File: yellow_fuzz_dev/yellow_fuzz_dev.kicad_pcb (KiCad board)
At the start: 2 copper layers, 148 parts, among them CON1 SN49B12B, J1 PJ-202A, J2 RA49B11, Q1 DMN2041L, Q10 BC817-25-TP, Q11 NSVJ3910SB3T1GOSCT-ND, Q12 BC817-25-TP, Q13 BC817-25-TP, Q14 NSVJ3910SB3T1GOSCT-ND, Q2 NSVJ3910SB3T1GOSCT-ND, Q3 DMN2041L, Q4 NSVJ3910SB3T1GOSCT-ND, Q5 BC817-25-TP, Q6 BC817-25-TP, Q7 BC817-25-TP, Q8 BC817-25-TP, Q9 BC817-25-TP, SW1 SW_SP3T_A24JP, SW2 SW_SP3T_A24JP, SW3 SW_SP3T_A24JP, SW4 SW_SPST_A11JP, SW5 SW_SPST_A11JP, U1 TL072CP, U2 TL072CP, U3 TL072CP, U4 TL072CP

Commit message: added 3d to connector and DIP footprints, moved to project lib, updated PCB
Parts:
- removed CON1: SN49B12B, digikey:Headphone_Jack_6.35mm_SN49B12B
- removed POT2, POT3: 3362P-1-102TLF, yellow_fuzz_dev:3362P-1-102TLF
- added C1: 1u, Capacitor_THT:CP_Radial_D4.0mm_P1.50mm, F.Cu at (350.5, 99.1)
- added C11: 100u, Capacitor_THT:CP_Radial_D5.0mm_P2.00mm, F.Cu at (330.9, 106.1)
- added C12: 100u, Capacitor_THT:CP_Radial_D5.0mm_P2.00mm, F.Cu at (337.5, 99.6)
- added C15: 10u, Capacitor_THT:CP_Radial_D5.0mm_P2.00mm, F.Cu at (330.9, 112.7)
- added C17: 10u, Capacitor_THT:CP_Radial_D5.0mm_P2.00mm, F.Cu at (337.5, 106.1)
- added C19: 1u, Capacitor_THT:CP_Radial_D4.0mm_P1.50mm, F.Cu at (356.1, 99.1)
- added C22: 220n, Capacitor_THT:CP_Radial_D5.0mm_P2.00mm, F.Cu at (344.2, 99.6)
- added C26: 1u, Capacitor_THT:CP_Radial_D4.0mm_P1.50mm, F.Cu at (350.5, 104.6)
- added C34: 10u, Capacitor_THT:CP_Radial_D5.0mm_P2.00mm, F.Cu at (337.5, 112.7)
- added C36: 1u, Capacitor_THT:CP_Radial_D4.0mm_P1.50mm, F.Cu at (343.9, 112.2)
- added C37: 10u, Capacitor_THT:CP_Radial_D5.0mm_P2.00mm, F.Cu at (344.2, 106.1)
- added C38: 220n, Capacitor_THT:CP_Radial_D5.0mm_P2.00mm, F.Cu at (354.9, 105.6)
- added C43: 1u, Capacitor_THT:CP_Radial_D4.0mm_P1.50mm, F.Cu at (354.6, 111.7)
- added C46: 1u, Capacitor_THT:CP_Radial_D4.0mm_P1.50mm, F.Cu at (360.2, 111.7)
- added C50: 10u, Capacitor_THT:CP_Radial_D5.0mm_P2.00mm, F.Cu at (361.6, 105.6)
- added C8: 100u, Capacitor_THT:CP_Radial_D5.0mm_P2.00mm, F.Cu at (330.9, 99.6)
- added J3: SN49B12B, yellow_fuzz_dev:Headphone_Jack_6.35mm_SN49B12B, F.Cu at (333.3, 28.1)
- added P3: 3362P-1-102TLF, yellow_fuzz_dev:3362PT, F.Cu at (108.0, 22.9)
- added P4: 3362P-1-102TLF, yellow_fuzz_dev:3362PT, F.Cu at (108.0, 31.6)
- BAT1: footprint digikey:Battery_Holder_9V_BC9VPC-ND -> yellow_fuzz_dev:Battery_Holder_9V_BC9VPC-ND
- J1: footprint digikey:Barrel_Jack_5.5mmODx2.1mmID_PJ-202A -> yellow_fuzz_dev:Barrel_Jack_5.5mmODx2.1mmID_PJ-202A
- S1: footprint digikey:Switch_Tactile_THT_6x6mm -> yellow_fuzz_dev:Switch_Tactile_THT_6x6mm
- U1, U2, U3, U4: footprint digikey:DIP-8_W7.62mm -> yellow_fuzz_dev:DIP-8_W7.62mm
- moved J2 307.4 mm to (382.3, 78.7), turned to 0 degrees
- moved S1 215.4 mm to (83.8, 31.6)
- moved U4 196.7 mm to (94.4, 43.2)
- moved U2 189.1 mm to (94.4, 20.3)
- moved U3 183.1 mm to (83.5, 43.2)
- moved U1 175.7 mm to (83.5, 20.3)
- moved BAT1 159.3 mm to (233.7, 153.7), turned to 0 degrees
- moved J1 118.4 mm to (386.0, -0.71)
- renumbered POT1 to P1, RV1 to P2, RV2 to P5, RV3 to P6, RV4 to P7, RV5 to P8, RV6 to P9

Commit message: placement partially done
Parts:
- P2: value R_POT_US -> PTV112-4420A-A104; footprint Potentiometer_THT:Potentiometer_Bourns_PTV09A-1_Single_Vertical -> yellow_fuzz_dev:Potentiometer_Bourns_PTV112_3417A_Dual_Vertical
- P5, P6, P7: value R_POT_US -> PTV111-4420A-A104
- P8: value R_POT_Dual_Separate -> PTV112-4420A-A503
- P9: value R_POT_US -> PTV111-4420A-A503; footprint yellow_fuzz_dev:Potentiometer_Bourns_PCW1J_R24_B_Single_Vertical -> yellow_fuzz_dev:Potentiometer_Bourns_PTV111_4420A_Single_Vertical
- moved C15 323.9 mm to (30.5, 233.7)
- moved R19 298.4 mm to (40.6, 256.5)
- moved R20 295.0 mm to (30.5, 246.4)
- moved C17 290.8 mm to (78.7, 238.8)
- moved C13 289.3 mm to (40.6, 243.8)
- moved J2 288.3 mm to (94.0, 76.2), turned to 180 degrees
- moved C19 281.0 mm to (116.8, 246.4)
- moved C14 279.2 mm to (39.8, 248.9)
- moved R21 277.5 mm to (30.5, 241.3)
- moved R17 277.4 mm to (39.8, 233.7)
- moved R3 275.4 mm to (76.2, 294.6)
- moved R13 273.1 mm to (61.0, 228.6)
- moved C26 269.8 mm to (83.8, 63.5), turned to 90 degrees
- moved Q6 268.3 mm to (94.0, 292.1)
- moved R18 267.7 mm to (40.6, 238.8)
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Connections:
- P2 pad 2: Net-(C16-Pad1) -> Net-(P2-Pad2)
- P2 pad 3: Net-(C16-Pad1) -> Net-(P2-Pad2)
- P5 pad 4: (no net) -> GND
- P6 pad 4: (no net) -> Net-(P6-Pad4)
- P7 pad 4: (no net) -> GND
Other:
- board outline added: 119.4 x 149.9 mm
- net class Default: clearance 0.2 -> 0.2032; trace_width 0.25 -> 0.2032; via_dia 0.8 -> 0.8128; via_drill 0.4 -> 0.4064
- rule trace_clearance: 0.2 -> 0.2032

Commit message: first draft placement done. Added ampharos logo.
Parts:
- added G***: LOGO, yellow_fuzz_dev:amph_1_5x1_5, F.Cu at (175.6, 180.8)
- moved R37 243.7 mm to (95.2, 181.4), turned to 180 degrees
- moved R47 243.4 mm to (95.2, 187.5), turned to 180 degrees
- moved R50 242.6 mm to (100.6, 175.3), turned to 180 degrees
- moved C35 242.5 mm to (100.6, 177.3)
- moved R39 237.8 mm to (100.6, 179.3)
- moved R42 237.7 mm to (95.2, 183.4)
- moved C28 237.6 mm to (95.2, 185.4)
- moved R46 237.4 mm to (100.6, 181.4)
- moved C33 237.3 mm to (100.6, 183.4)
- moved Q10 237.2 mm to (95.5, 190.8), turned to 180 degrees
- moved Q12 236.6 mm to (100.8, 190.8)
- moved C29 233.3 mm to (100.6, 185.4)
- moved C31 233.0 mm to (100.6, 187.5)
- moved R49 232.7 mm to (100.6, 173.2)
- moved R41 230.3 mm to (95.2, 177.3)
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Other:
- board size 119.4 x 149.9 mm -> 121.9 x 149.9 mm
- board text added: "1.5 kHz"
- board text added: "333 Hz"
- board text added: "CLIP D1"
- board text added: "CLIP D2"
- board text added: "CLIP R1"
- board text added: "CLIP R2"
- board text added: "DIST"
- board text added: "FUZZ ME UP"
- board text added: "GAIN"
- board text added: "Graduator Dev May 2020"
- board text added: "HIGH"
- board text added: "INPUT"
- board text added: "LED GE SI"
- board text added: "LEVEL"
- board text added: "LOW"
- board text added: "MID"
- board text added: "MID f"
- board text added: "MOD STOCK OFF"
- board text added: "OFF"
- board text added: "ON"
- board text added: "OUTPUT"
- board text added: "POST FILTERS"
- board text added: "PREBOOST FILTER"

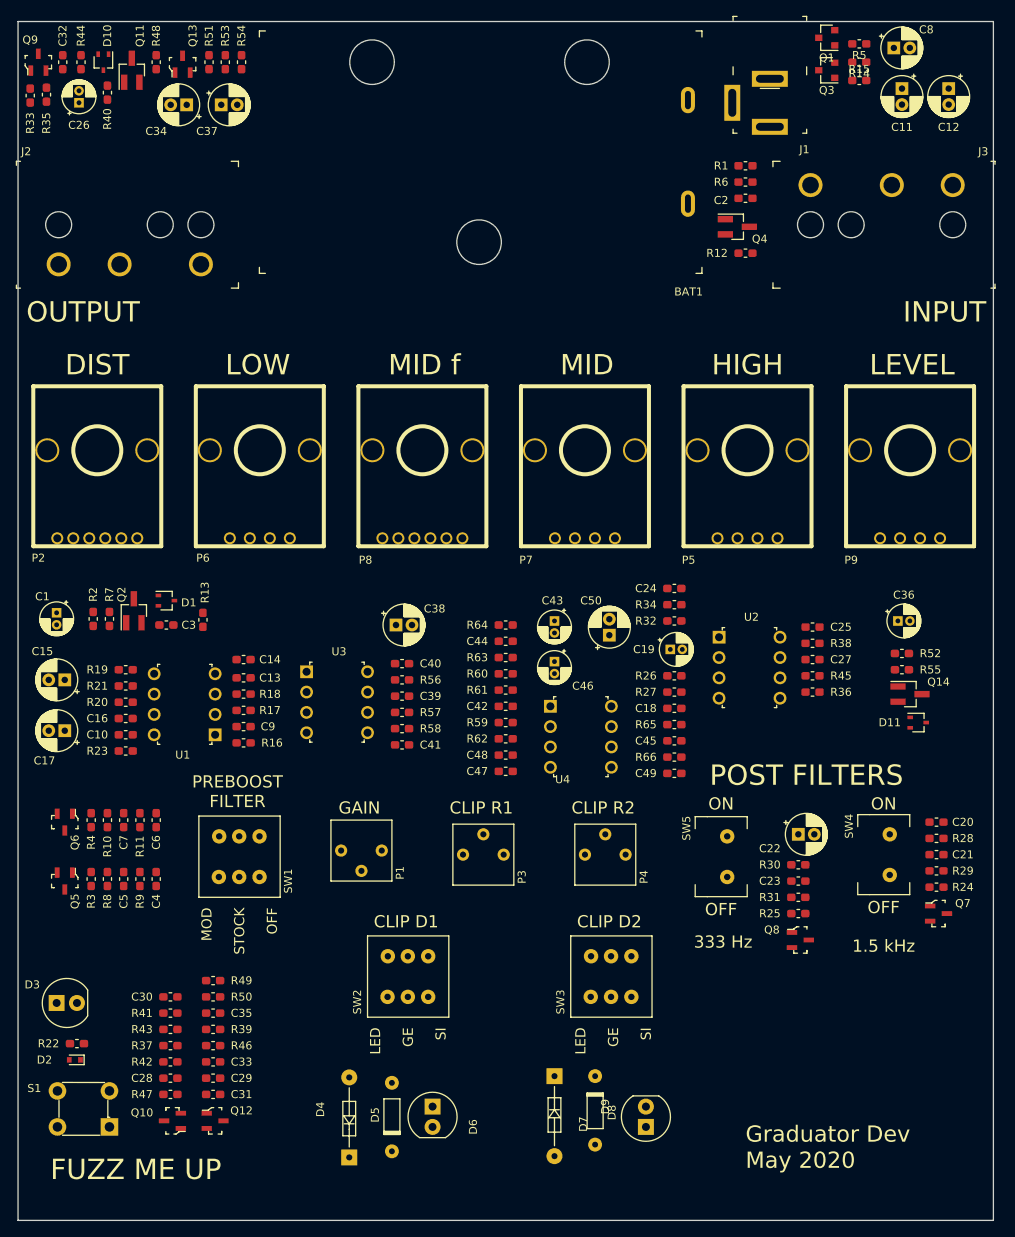
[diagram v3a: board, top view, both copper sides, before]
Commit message: did a bunch of routing and rounded the corners
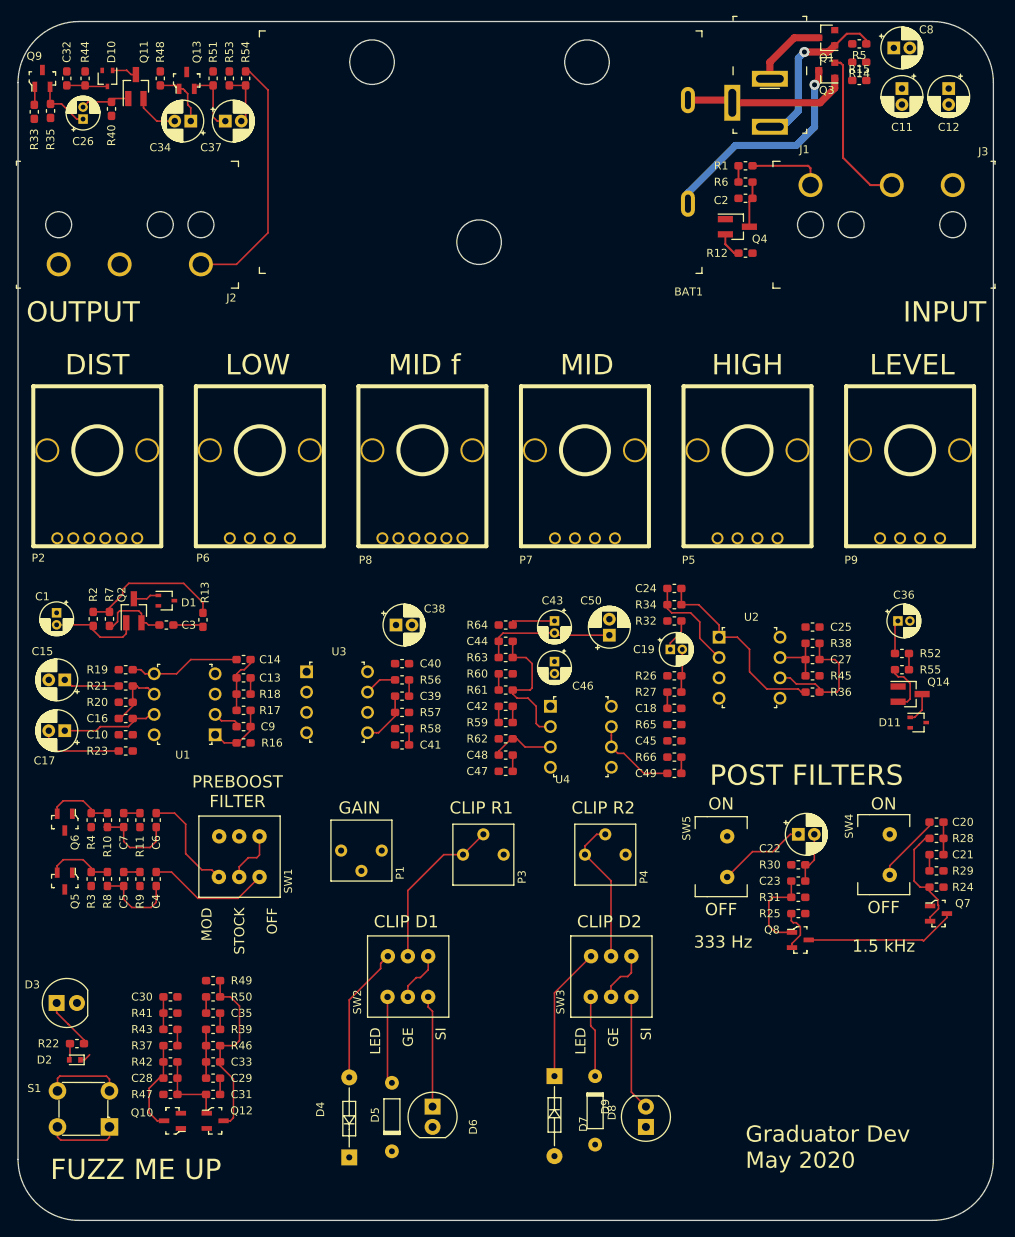
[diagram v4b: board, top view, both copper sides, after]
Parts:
- moved C34 2.09 mm to (97.8, 65.8)
- moved C37 2.09 mm to (102.1, 65.8)
- moved Q11 2.09 mm to (90.9, 61.5)
- moved Q13 2.09 mm to (97.3, 60.7)
- moved R33 2.09 mm to (78.2, 64.6)
- moved R35 2.09 mm to (80.3, 64.5)
- moved R40 2.09 mm to (87.9, 64.3)
- moved C26 2.09 mm to (84.3, 65.5)
- moved C32 2.09 mm to (82.3, 60.5)
- moved D10 2.09 mm to (87.4, 60.5)
- moved Q9 2.09 mm to (79.2, 60.5)
- moved R48 2.09 mm to (94.0, 60.5)
- moved R51 2.09 mm to (100.6, 60.5)
- moved R44 2.09 mm to (84.6, 60.5)
- moved R53 2.09 mm to (102.6, 60.5)
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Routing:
- net Net-(J2-PadT): track 0.00 -> 31.6 mm
- net Net-(BAT1-PadNEG): track 0.00 -> 27.9 mm, vias 0 -> 1
- net Net-(C24-Pad1): track 0.00 -> 24.6 mm
- net /DIST_IN_EN: track 0.00 -> 23.0 mm
- net Net-(J1-Pad1): track 0.00 -> 23.0 mm, vias 0 -> 1
- net +9V: track 0.00 -> 22.5 mm
- net +4V: track 0.00 -> 22.2 mm
- net Net-(P3-Pad1): track 0.00 -> 20.6 mm
- net Net-(BAT1-PadPOS): track 0.00 -> 20.5 mm
- net /INPUT_RING: track 0.00 -> 20.2 mm
- net Net-(C44-Pad2): track 0.00 -> 18.5 mm
- net Net-(P4-Pad1): track 0.00 -> 18.3 mm
- net Net-(D4-Pad2): track 0.00 -> 17.1 mm
- net Net-(D7-Pad1): track 0.00 -> 16.9 mm
- net /tone_block/TONE_OUT: track 0.00 -> 16.7 mm
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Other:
- outline, holes or cut-outs redrawn

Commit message: routing complete and DRC clear
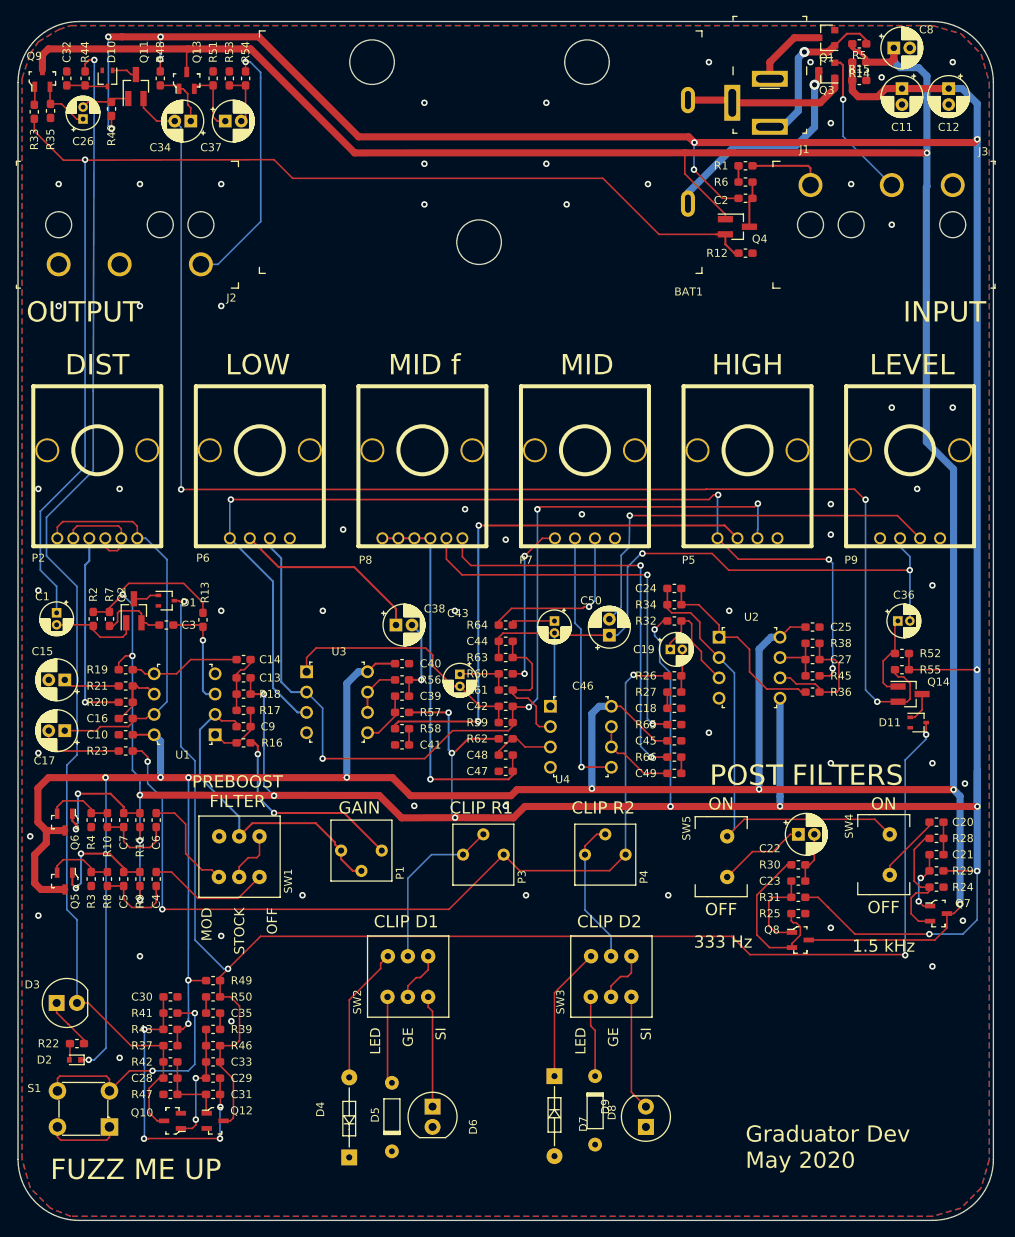
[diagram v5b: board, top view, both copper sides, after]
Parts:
- moved C43 11.9 mm to (131.4, 134.9)
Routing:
- net +4V: track 22.2 -> 559.5 mm, vias 0 -> 24
- net +9V: track 22.5 -> 556.2 mm, vias 0 -> 12
- net /DIST_IN_EN: track 23.0 -> 192.5 mm, vias 0 -> 4
- net Net-(C34-Pad2): track 12.2 -> 173.2 mm, vias 0 -> 3
- net /BUFFERED_IN: track 3.34 -> 157.7 mm, vias 0 -> 1
- net /BYPASS_EN: track 11.7 -> 150.0 mm, vias 0 -> 1
- net /tone_block/TONE_IN: track 0.00 -> 128.8 mm, vias 0 -> 4
- net Net-(C42-Pad2): track 2.03 -> 118.8 mm, vias 0 -> 4
- net Net-(P3-Pad3): track 0.00 -> 111.6 mm, vias 0 -> 3
- net Net-(P5-Pad2): track 0.00 -> 68.6 mm, vias 0 -> 2
- net /tone_block/TONE_OUT: track 16.7 -> 83.8 mm, vias 0 -> 2
- net Net-(P8-Pad6): track 0.00 -> 51.6 mm, vias 0 -> 2
- net Net-(C50-Pad2): track 0.00 -> 51.4 mm, vias 0 -> 1
- net Net-(P8-Pad3): track 0.00 -> 49.6 mm, vias 0 -> 2
- net Net-(C47-Pad1): track 2.03 -> 49.1 mm, vias 0 -> 1
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- added copper zone on B.Cu, net GND
- added copper zone on F.Cu, net GND
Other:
- rule trace_min: 0.2 -> 0.2032

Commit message: corrected BOM fields and generated BOM
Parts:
- removed G***: LOGO, yellow_fuzz_dev:amph_1_5x1_5

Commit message: generated gerbers, BOM, and sch - releasing dev to fab
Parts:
- added G***: LOGO, yellow_fuzz_dev:amph_1_5x1_5, F.Cu at (177.0, 180.8)
